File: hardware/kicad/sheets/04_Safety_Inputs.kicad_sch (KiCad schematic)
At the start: 0 parts

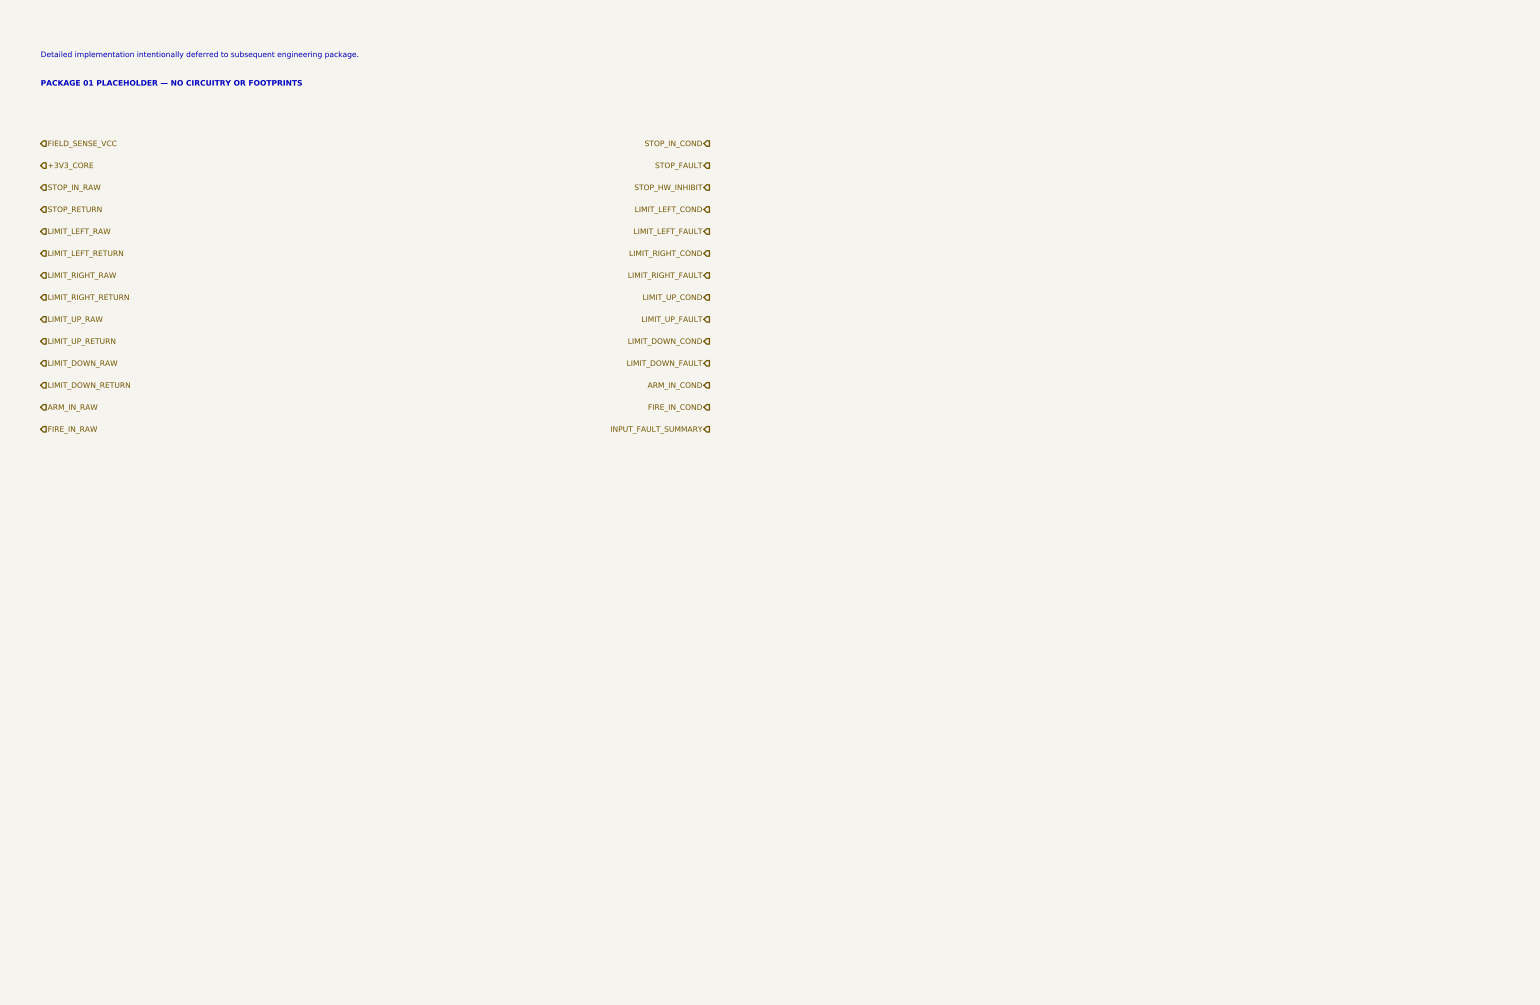
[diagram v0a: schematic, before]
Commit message: Implement supervised safety input subsystem
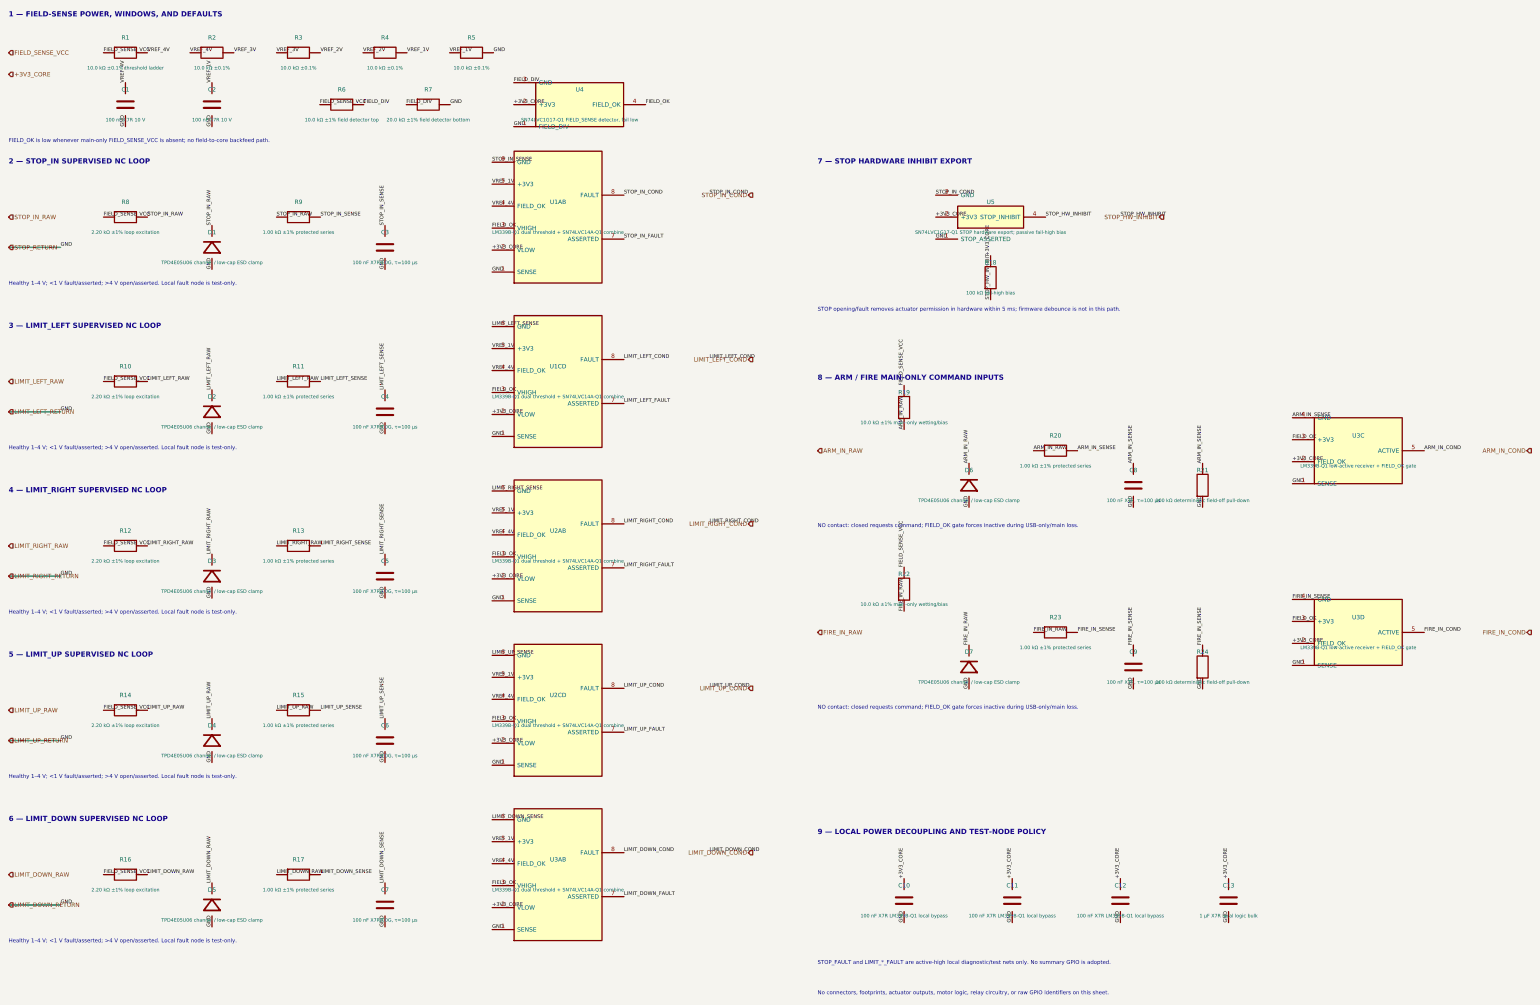
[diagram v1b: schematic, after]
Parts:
- added C1, C2: 100 nF X7R 10 V, symbol IPC100:C
- added C10, C11, C12: 100 nF X7R LM339B-Q1 local bypass, symbol IPC100:C
- added C13: 1 µF X7R local logic bulk, symbol IPC100:C
- added C3, C4, C5, C6, C7: 100 nF X7R/C0G, τ=100 µs, symbol IPC100:C
- added C8, C9: 100 nF X7R, τ=100 µs, symbol IPC100:C
- added D1, D2, D3, D4, D5, D6, D7: TPD4E05U06 channel / low-cap ESD clamp, symbol IPC100:D
- added R1: 10.0 kΩ ±0.1% threshold ladder, symbol IPC100:R
- added R10, R12, R14, R16, R8: 2.20 kΩ ±1% loop excitation, symbol IPC100:R
- added R11, R13, R15, R17, R20, R23, R9: 1.00 kΩ ±1% protected series, symbol IPC100:R
- added R18: 100 kΩ fail-high bias, symbol IPC100:R
- added R19, R22: 10.0 kΩ ±1% main-only wetting/bias, symbol IPC100:R
- added R2, R3, R4, R5: 10.0 kΩ ±0.1%, symbol IPC100:R
- added R21, R24: 100 kΩ deterministic field-off pull-down, symbol IPC100:R
- added R6: 10.0 kΩ ±1% field detector top, symbol IPC100:R
- added R7: 20.0 kΩ ±1% field detector bottom, symbol IPC100:R
- added U1AB, U1CD, U2AB, U2CD, U3AB: LM339B-Q1 dual threshold + SN74LVC14A-Q1 combine, symbol IPC100:WINDOW
- added U3C, U3D: LM339B-Q1 low-active receiver + FIELD_OK gate, symbol IPC100:CMDREC
- added U4: SN74LVC1G17-Q1 FIELD_SENSE detector, fail low, symbol IPC100:FIELDDET
- added U5: SN74LVC1G17-Q1 STOP hardware export; passive fail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, symbol IPC100:SAFEBUF
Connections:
- net +3V3_CORE: now also C10.2, C11.2, C12.2, C13.2, R18.2, U1AB.2 (VLOW), U1CD.2 (VLOW), U2AB.2 (VLOW), U2CD.2 (VLOW), U3AB.2 (VLOW), U3C.2 (FIELD_OK), U3D.2 (FIELD_OK), U4.2 (+3V3), U5.2 (+3V3)
- net ARM_IN_COND: now also U3C.5 (ACTIVE)
- net ARM_IN_RAW: now also D6.2, R19.1, R20.1
- net FIELD_SENSE_VCC: now also R1.1, R10.1, R12.1, R14.1, R16.1, R19.2, R22.2, R6.1, R8.1
- net FIRE_IN_COND: now also U3D.5 (ACTIVE)
- net FIRE_IN_RAW: now also D7.2, R22.1, R23.1
- net LIMIT_DOWN_COND: now also U3AB.8 (FAULT)
- net LIMIT_DOWN_FAULT: now also U3AB.7 (ASSERTED)
- net LIMIT_DOWN_RAW: now also D5.2, R16.2, R17.1
- net LIMIT_DOWN_RETURN: now also C1.1, C10.1, C11.1, C12.1, C13.1, C2.1, C3.1, C4.1, C5.1, C6.1, C7.1, C8.1, C9.1, D1.1, D2.1, D3.1, D4.1, D5.1, D6.1, D7.1, R21.1, R24.1, R5.2, R7.2, U1AB.1 (SENSE), U1CD.1 (SENSE), U2AB.1 (SENSE), U2CD.1 (SENSE), U3AB.1 (SENSE), U3C.1 (SENSE), U3D.1 (SENSE), U4.1 (FIELD_DIV), U5.1 (STOP_ASSERTED)
- net LIMIT_LEFT_COND: now also U1CD.8 (FAULT)
- net LIMIT_LEFT_FAULT: now also U1CD.7 (ASSERTED)
- net LIMIT_LEFT_RAW: now also D2.2, R10.2, R11.1
- net LIMIT_RIGHT_COND: now also U2AB.8 (FAULT)
- net LIMIT_RIGHT_FAULT: now also U2AB.7 (ASSERTED)
- net LIMIT_RIGHT_RAW: now also D3.2, R12.2, R13.1
- net LIMIT_UP_COND: now also U2CD.8 (FAULT)
- net LIMIT_UP_FAULT: now also U2CD.7 (ASSERTED)
- net LIMIT_UP_RAW: now also D4.2, R14.2, R15.1
- net STOP_HW_INHIBIT: now also R18.1, U5.4 (STOP_INHIBIT)
- net STOP_IN_COND: now also U1AB.8 (FAULT), U5.3 (GND)
- net STOP_IN_RAW: now also D1.2, R8.2, R9.1
- new net ARM_IN_SENSE: C8.2, R20.2, R21.2, U3C.4 (GND)
- new net FIELD_DIV: R6.2, R7.1, U4.3 (GND)
- new net FIELD_OK: U1AB.3 (VHIGH), U1CD.3 (VHIGH), U2AB.3 (VHIGH), U2CD.3 (VHIGH), U3AB.3 (VHIGH), U3C.3 (+3V3), U3D.3 (+3V3), U4.4 (FIELD_OK)
- new net FIRE_IN_SENSE: C9.2, R23.2, R24.2, U3D.4 (GND)
- new net LIMIT_DOWN_SENSE: C7.2, R17.2, U3AB.6 (GND)
- new net LIMIT_LEFT_SENSE: C4.2, R11.2, U1CD.6 (GND)
- new net LIMIT_RIGHT_SENSE: C5.2, R13.2, U2AB.6 (GND)
- new net LIMIT_UP_SENSE: C6.2, R15.2, U2CD.6 (GND)
- new net STOP_IN_FAULT: U1AB.7 (ASSERTED)
- new net STOP_IN_SENSE: C3.2, R9.2, U1AB.6 (GND)
- new net VREF_1V: C2.2, R4.2, R5.1, U1AB.5 (+3V3), U1CD.5 (+3V3), U2AB.5 (+3V3), U2CD.5 (+3V3), U3AB.5 (+3V3)
- new net VREF_2V: R3.2, R4.1
- new net VREF_3V: R2.2, R3.1
- new net VREF_4V: C1.2, R1.2, R2.1, U1AB.4 (FIELD_OK), U1CD.4 (FIELD_OK), U2AB.4 (FIELD_OK), U2CD.4 (FIELD_OK), U3AB.4 (FIELD_OK)
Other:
- note added: "1 — FIELD-SENSE POWER, WINDOWS, AND DEFAULTS"
- note added: "2 — STOP_IN SUPERVISED NC LOOP"
- note added: "3 — LIMIT_LEFT SUPERVISED NC LOOP"
- note added: "4 — LIMIT_RIGHT SUPERVISED NC LOOP"
- note added: "5 — LIMIT_UP SUPERVISED NC LOOP"
- note added: "6 — LIMIT_DOWN SUPERVISED NC LOOP"
- note added: "7 — STOP HARDWARE INHIBIT EXPORT"
- note added: "8 — ARM / FIRE MAIN-ONLY COMMAND INPUTS"
- note added: "9 — LOCAL POWER DECOUPLING AND TEST-NODE POLICY"
- note added: "FIELD_OK is low whenever main-only FIELD_SENSE_VCC is absent; no field-to-core backfeed path."
- note added: "Healthy 1–4 V; <1 V fault/asserted; >4 V open/asserted. Local fault node is test-only."
- note added: "NO contact: closed requests command; FIELD_OK gate forces inactive during USB-only/main loss."
- note added: "No connectors, footprints, actuator outputs, motor logic, relay circuitry, or raw GPIO identifiers on this sheet."
- note added: "STOP opening/fault removes actuator permission in hardware within 5 ms; firmware debounce is not in this path."
- note added: "STOP_FAULT and LIMIT_*_FAULT are active-high local diagnostic/test nets only. No summary GPIO is adopted."
- note removed: "Detailed implementation intentionally deferred to subsequent engineering package."
- note removed: "PACKAGE 01 PLACEHOLDER — NO CIRCUITRY OR FOOTPRINTS"

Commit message: Normalize Rev A reference designators
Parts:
- renumbered C1 to C401, C2 to C402, C3 to C403, C4 to C404, C5 to C405, C6 to C406, C7 to C407, C8 to C408, C9 to C409, C10 to C410, C11 to C411, C12 to C412, C13 to C413, D1 to D401, D2 to D402, D3 to D403, D4 to D404, D5 to D405, D6 to D406, D7 to D407, R1 to R401, R2 to R402, R3 to R403, R4 to R404, R5 to R405, R6 to R406, R7 to R407, R8 to R408, R9 to R409, R10 to R410, R11 to R411, R12 to R412, R13 to R413, R14 to R414, R15 to R415, R16 to R416, R17 to R417, R18 to R418, R19 to R419, R20 to R420, R21 to R421, R22 to R422, R23 to R423, R24 to R424, U1AB to U401AB, U1CD to U401CD, U2AB to U402AB, U2CD to U402CD, U3AB to U403AB, U3C to U403C, U3D to U403D, U4 to U404, U5 to U405

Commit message: Physically decompose Sheet 04 safety inputs
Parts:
- removed U401AB, U401CD, U402AB, U402CD, U403AB: LM339B-Q1 dual threshold + SN74LVC14A-Q1 combine, symbol IPC100:WINDOW
- removed U403C, U403D: LM339B-Q1 low-active receiver + FIELD_OK gate, symbol IPC100:CMDREC
- removed U404: SN74LVC1G17-Q1 FIELD_SENSE detector, fail low, symbol IPC100:FIELDDET
- removed U405: SN74LVC1G17-Q1 STOP hardware export; passive fail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, symbol IPC100:SAFEBUF
- added C414: 100 nF X7R midpoint filter, symbol IPC100:C
- added C415, C416, C417, C418, C419, C420, C421, C422, C423, C424, C425, C426: 10 nF X7R local threshold filter, symbol IPC100:C
- added C427, C428, C429: 100 nF X7R package-local bypass, symbol IPC100:C
- added C430: 100 nF X7R U404 local bypass, symbol IPC100:C
- added C431: 100 nF X7R U405 local bypass, symbol IPC100:C
- added R425: 10.0 kΩ ±0.1%, ≤25 ppm/°C midpoint top, symbol IPC100:R
- added R426: 10.0 kΩ ±0.1%, ≤25 ppm/°C midpoint bottom, symbol IPC100:R
- added R427, R428, R429, R430, R431, R432, R433, R434, R435, R436, R437, R438: 10.0 kΩ ±0.1% reference isolation, symbol IPC100:R
- added R439, R440, R441, R442, R443, R444, R445, R446, R447, R448, R449, R450: 499 kΩ ±1% external hysteresis, symbol IPC100:R
- added R451, R452, R453, R454, R455, R456, R457: 10.0 kΩ ±1% open-drain pull-up, symbol IPC100:R
- added R458, R459, R460, R461, R462: 100 kΩ fail-low qualifier bias, symbol IPC100:R
- added R463, R464: 100 kΩ fail-low ACTIVE bias, symbol IPC100:R
- added TP401: STOP_IN_RAW, symbol IPC100:TP
- added TP402: STOP_IN_SENSE, symbol IPC100:TP
- added TP403: STOP_WINDOW_OK, symbol IPC100:TP
- added TP404: STOP_ASSERTED, symbol IPC100:TP
- added TP405: STOP_FAULT, symbol IPC100:TP
- added TP406: LIMIT_LEFT_RAW, symbol IPC100:TP
- added TP407: LIMIT_LEFT_SENSE, symbol IPC100:TP
- added TP408: LEFT_WINDOW_OK, symbol IPC100:TP
- added TP409: LEFT_ASSERTED, symbol IPC100:TP
- added TP410: LIMIT_LEFT_FAULT, symbol IPC100:TP
- added TP411: LIMIT_RIGHT_RAW, symbol IPC100:TP
- added TP412: LIMIT_RIGHT_SENSE, symbol IPC100:TP
- added TP413: RIGHT_WINDOW_OK, symbol IPC100:TP
- added TP414: RIGHT_ASSERTED, symbol IPC100:TP
- added TP415: LIMIT_RIGHT_FAULT, symbol IPC100:TP
- added TP416: LIMIT_UP_RAW, symbol IPC100:TP
- added TP417: LIMIT_UP_SENSE, symbol IPC100:TP
- added TP418: UP_WINDOW_OK, symbol IPC100:TP
- added TP419: UP_ASSERTED, symbol IPC100:TP
- added TP420: LIMIT_UP_FAULT, symbol IPC100:TP
- added TP421: LIMIT_DOWN_RAW, symbol IPC100:TP
- added TP422: LIMIT_DOWN_SENSE, symbol IPC100:TP
- added TP423: DOWN_WINDOW_OK, symbol IPC100:TP
- added TP424: DOWN_ASSERTED, symbol IPC100:TP
- added TP425: LIMIT_DOWN_FAULT, symbol IPC100:TP
- added TP426: STOP_HW_INHIBIT, symbol IPC100:TP
- added TP427: ARM_IN_RAW, symbol IPC100:TP
- added TP428: ARM_IN_SENSE, symbol IPC100:TP
- added TP429: ARM_REQUEST_OK, symbol IPC100:TP
- added TP430: ARM_ACTIVE, symbol IPC100:TP
- added TP431: FIRE_IN_RAW, symbol IPC100:TP
- added TP432: FIRE_IN_SENSE, symbol IPC100:TP
- added TP433: FIRE_REQUEST_OK, symbol IPC100:TP
- added TP434: FIRE_ACTIVE, symbol IPC100:TP
- added TP435: VREF_1V, symbol IPC100:TP
- added TP436: VREF_4V, symbol IPC100:TP
- added TP437: VREF_2V5, symbol IPC100:TP
- added TP438: FIELD_OK, symbol IPC100:TP
- added U404: SN74LVC1G17QDBVRQ1 FIELD_OK, symbol IPC100:SN74LVC1G17QDBVRQ1
- added U405: SN74LVC1G17QDBVRQ1 STOP export, symbol IPC100:SN74LVC1G17QDBVRQ1
- added U406, U407, U408: TLV7044QPWRQ1, symbol IPC100:TLV7044QPWRQ1
- added U409, U410: SN74LVC08AQPWRQ1, symbol IPC100:SN74LVC08AQPWRQ1
- added U411: SN74LVC14AQPWRQ1, symbol IPC100:SN74LVC14AQPWRQ1
- C401, C402: value 100 nF X7R 10 V -> 100 nF X7R reference filter
- C408, C409: value 100 nF X7R, τ=100 µs -> 100 nF X7R input filter
- C410, C411, C412: value 100 nF X7R LM339B-Q1 local bypass -> 100 nF X7R package-local bypass
- R401: value 10.0 kΩ ±0.1% threshold ladder -> 10.0 kΩ ±0.1%, ≤25 ppm/°C ladder
- R402, R403, R404, R405: value 10.0 kΩ ±0.1% -> 10.0 kΩ ±0.1%, ≤25 ppm/°C ladder
- R406: value 10.0 kΩ ±1% field detector top -> 10.0 kΩ ±1% FIELD_OK top
- R407: value 20.0 kΩ ±1% field detector bottom -> 10.0 kΩ ±1% FIELD_OK bottom; POR ordering
- R419, R422: value 10.0 kΩ ±1% main-only wetting/bias -> 10.0 kΩ ±1% main-only wetting
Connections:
- net +3V3_CORE: now also C413.1, R418.1, C427.1, C428.1, C429.1, C430.1, C431.1, R451.1, R452.1, R453.1, R454.1, R455.1, R456.1, R457.1, U404.3 (GND), U405.3 (GND), U409.7 (GND), U410.7 (GND), U411.7 (GND); no longer C410.2, C411.2, C412.2, C413.2, R418.2
- net ARM_IN_COND: now also R463.1, TP430.1 (TP), U410.6 (Y)
- net ARM_IN_RAW: now also D406.1, R419.2, TP427.1 (TP); no longer D406.2, R419.1
- net ARM_IN_SENSE: now also C408.1, R421.1, TP428.1 (TP), U407.13 (IN-); no longer C408.2, R421.2
- net FIELD_DIV: now also U404.2 (A)
- net FIELD_OK: now also TP438.1 (TP), U404.4 (Y), U409.1 (A), U409.12 (A), U409.4 (A), U409.9 (A), U410.1 (A), U410.4 (A), U410.9 (A)
- net FIELD_SENSE_VCC: now also C410.1, C411.1, C412.1, R419.1, R422.1, R425.1, U406.11 (VEE), U407.11 (VEE), U408.11 (VEE); no longer R419.2, R422.2
- net FIRE_IN_COND: now also R464.1, TP434.1 (TP), U410.8 (Y)
- net FIRE_IN_RAW: now also D407.1, R422.2, TP431.1 (TP); no longer D407.2, R422.1
- net FIRE_IN_SENSE: now also C409.1, R424.1, TP432.1 (TP), U408.13 (IN-); no longer C409.2, R424.2
- net LIMIT_DOWN_COND: now also TP424.1 (TP), TP425.1 (TP), U411.10 (Y)
- net LIMIT_DOWN_RAW: now also D405.1, TP421.1 (TP); no longer D405.2
- net LIMIT_DOWN_RETURN: no longer C401.1, C402.1, C403.1, C404.1, C405.1, C406.1, C407.1, C408.1, C409.1, C410.1, C411.1, C412.1, C413.1, D401.1, D402.1, D403.1, D404.1, D405.1, D406.1, D407.1, R405.2, R407.2, R421.1, R424.1
- net LIMIT_DOWN_SENSE: now also C407.1, TP422.1 (TP), U406.12 (IN+), U408.9 (IN-); no longer C407.2
- net LIMIT_LEFT_COND: now also TP409.1 (TP), TP410.1 (TP), U411.4 (Y)
- net LIMIT_LEFT_RAW: now also D402.1, TP406.1 (TP); no longer D402.2
- net LIMIT_LEFT_SENSE: now also C404.1, TP407.1 (TP), U406.6 (IN-), U408.3 (IN+); no longer C404.2
- net LIMIT_RIGHT_COND: now also TP414.1 (TP), TP415.1 (TP), U411.6 (Y)
- net LIMIT_RIGHT_RAW: now also D403.1, TP411.1 (TP); no longer D403.2
- net LIMIT_RIGHT_SENSE: now also C405.1, TP412.1 (TP), U407.6 (IN-), U408.5 (IN+); no longer C405.2
- net LIMIT_UP_COND: now also TP419.1 (TP), TP420.1 (TP), U411.8 (Y)
- net LIMIT_UP_RAW: now also D404.1, TP416.1 (TP); no longer D404.2
- net LIMIT_UP_SENSE: now also C406.1, TP417.1 (TP), U406.9 (IN-), U407.10 (IN+); no longer C406.2
- net STOP_HW_INHIBIT: now also R418.2, TP426.1 (TP), U405.4 (Y); no longer R418.1
- net STOP_IN_COND: now also TP404.1 (TP), TP405.1 (TP), U405.2 (A), U411.2 (Y)
- net STOP_IN_RAW: now also D401.1, TP401.1 (TP); no longer D401.2
- net STOP_IN_SENSE: now also C403.1, TP402.1 (TP), U406.2 (IN-), U407.3 (IN+); no longer C403.2
- net VREF_1V: now also C402.1, R427.1, R429.1, R431.1, R433.1, R435.1, TP435.1 (TP); no longer C402.2
- net VREF_4V: now also C401.1, R428.1, R430.1, R432.1, R434.1, R436.1, TP436.1 (TP); no longer C401.2
- new net ARM_REQUEST_OK: R449.1, R456.2, TP429.1 (TP), U407.14 (OUT), U410.5 (B)
- new net ARM_VMID: C425.1, R437.2, R449.2, U407.12 (IN+)
- new net DOWN_QUAL_OK: R462.1, U410.3 (Y), U411.11 (A)
- new net DOWN_VHIGH: C424.1, R436.2, R448.2, U406.13 (IN-)
- new net DOWN_VLOW: C423.1, R435.2, R447.2, U408.10 (IN+)
- new net DOWN_WINDOW_OK: R447.1, R448.1, R455.2, TP423.1 (TP), U406.14 (OUT), U408.8 (OUT), U410.2 (B)
- new net FIRE_REQUEST_OK: R450.1, R457.2, TP433.1 (TP), U408.14 (OUT), U410.10 (B)
- new net FIRE_VMID: C426.1, R438.2, R450.2, U408.12 (IN+)
- new net GND: C401.2, C402.2, C403.2, C404.2, C405.2, C406.2, C407.2, C408.2, C409.2, C410.2, C411.2, C412.2, C413.2, C414.2, C415.2, C416.2, C417.2, C418.2, C419.2, C420.2, C421.2, C422.2, C423.2, C424.2, C425.2, C426.2, C427.2, C428.2, C429.2, C430.2, C431.2, D401.2, D402.2, D403.2, D404.2, D405.2, D406.2, D407.2, R405.2, R407.2, R421.2, R424.2, R426.2, R458.2, R459.2, R460.2, R461.2, R462.2, R463.2, R464.2, U404.5 (VCC), U405.5 (VCC), U406.4 (VCC), U407.4 (VCC), U408.4 (VCC), U409.14 (VCC), U410.12 (A), U410.13 (B), U410.14 (VCC), U411.13 (A), U411.14 (VCC)
- new net LEFT_QUAL_OK: R459.1, U409.6 (Y), U411.3 (A)
- new net LEFT_VHIGH: C418.1, R430.2, R442.2, U408.2 (IN-)
- new net LEFT_VLOW: C417.1, R429.2, R441.2, U406.5 (IN+)
- new net LEFT_WINDOW_OK: R441.1, R442.1, R452.2, TP408.1 (TP), U406.7 (OUT), U408.1 (OUT), U409.5 (B)
- new net RIGHT_QUAL_OK: R460.1, U409.8 (Y), U411.5 (A)
- new net RIGHT_VHIGH: C420.1, R432.2, R444.2, U408.6 (IN-)
- new net RIGHT_VLOW: C419.1, R431.2, R443.2, U407.5 (IN+)
- new net RIGHT_WINDOW_OK: R443.1, R444.1, R453.2, TP413.1 (TP), U407.7 (OUT), U408.7 (OUT), U409.10 (B)
- new net STOP_QUAL_OK: R458.1, U409.3 (Y), U411.1 (A)
- new net STOP_VHIGH: C416.1, R428.2, R440.2, U407.2 (IN-)
- new net STOP_VLOW: C415.1, R427.2, R439.2, U406.3 (IN+)
- new net STOP_WINDOW_OK: R439.1, R440.1, R451.2, TP403.1 (TP), U406.1 (OUT), U407.1 (OUT), U409.2 (B)
- new net U410_UNUSED_Y: U410.11 (Y)
- new net U411_UNUSED_Y: U411.12 (Y)
- new net UP_QUAL_OK: R461.1, U409.11 (Y), U411.9 (A)
- new net UP_VHIGH: C422.1, R434.2, R446.2, U407.9 (IN-)
- new net UP_VLOW: C421.1, R433.2, R445.2, U406.10 (IN+)
- new net UP_WINDOW_OK: R445.1, R446.1, R454.2, TP418.1 (TP), U406.8 (OUT), U407.8 (OUT), U409.13 (B)
- new net VREF_2V5: C414.1, R425.2, R426.1, R437.1, R438.1, TP437.1 (TP)
- no-connect marks 0 -> 2
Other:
- note added: "1 — FIELD-TRACKING REFERENCES AND FIELD VALIDITY"
- note added: "ARM — NO command receiver"
- note added: "DOWN — supervised NC window"
- note added: "FIRE — NO command receiver"
- note added: "LEFT — supervised NC window"
- note added: "PACKAGE POWER, DECOUPLING, UNUSED UNITS, AND SHARED DFT"
- note added: "RIGHT — supervised NC window"
- note added: "STOP — independent hardware inhibit export"
- note added: "STOP — supervised NC window"
- note added: "UP — supervised NC window"
- note removed: "1 — FIELD-SENSE POWER, WINDOWS, AND DEFAULTS"
- note removed: "2 — STOP_IN SUPERVISED NC LOOP"
- note removed: "3 — LIMIT_LEFT SUPERVISED NC LOOP"
- note removed: "4 — LIMIT_RIGHT SUPERVISED NC LOOP"
- note removed: "5 — LIMIT_UP SUPERVISED NC LOOP"
- note removed: "6 — LIMIT_DOWN SUPERVISED NC LOOP"
- note removed: "7 — STOP HARDWARE INHIBIT EXPORT"
- note removed: "8 — ARM / FIRE MAIN-ONLY COMMAND INPUTS"
- note removed: "9 — LOCAL POWER DECOUPLING AND TEST-NODE POLICY"
- note removed: "FIELD_OK is low whenever main-only FIELD_SENSE_VCC is absent; no field-to-core backfeed path."
- note removed: "Healthy 1–4 V; <1 V fault/asserted; >4 V open/asserted. Local fault node is test-only."
- note removed: "NO contact: closed requests command; FIELD_OK gate forces inactive during USB-only/main loss."
- note removed: "No connectors, footprints, actuator outputs, motor logic, relay circuitry, or raw GPIO identifiers on this sheet."
- note removed: "STOP opening/fault removes actuator permission in hardware within 5 ms; firmware debounce is not in this path."
- note removed: "STOP_FAULT and LIMIT_*_FAULT are active-high local diagnostic/test nets only. No summary GPIO is adopted."
